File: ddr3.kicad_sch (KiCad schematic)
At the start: 22 parts, among them U101 xc7z010clg400, U201 MT41K256M16TW-107_P

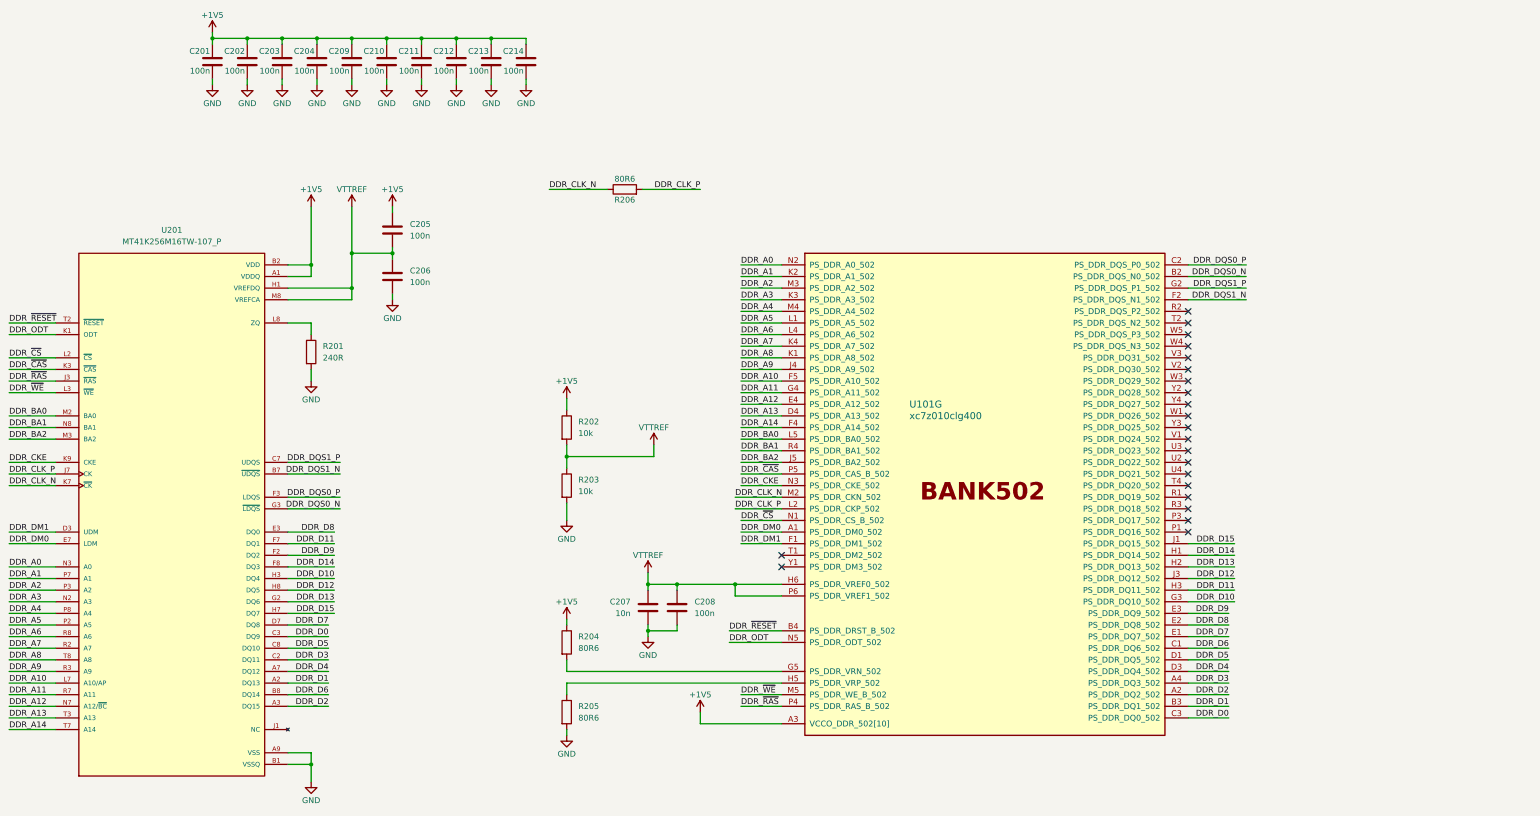
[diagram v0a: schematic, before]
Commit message: feat: add serial res
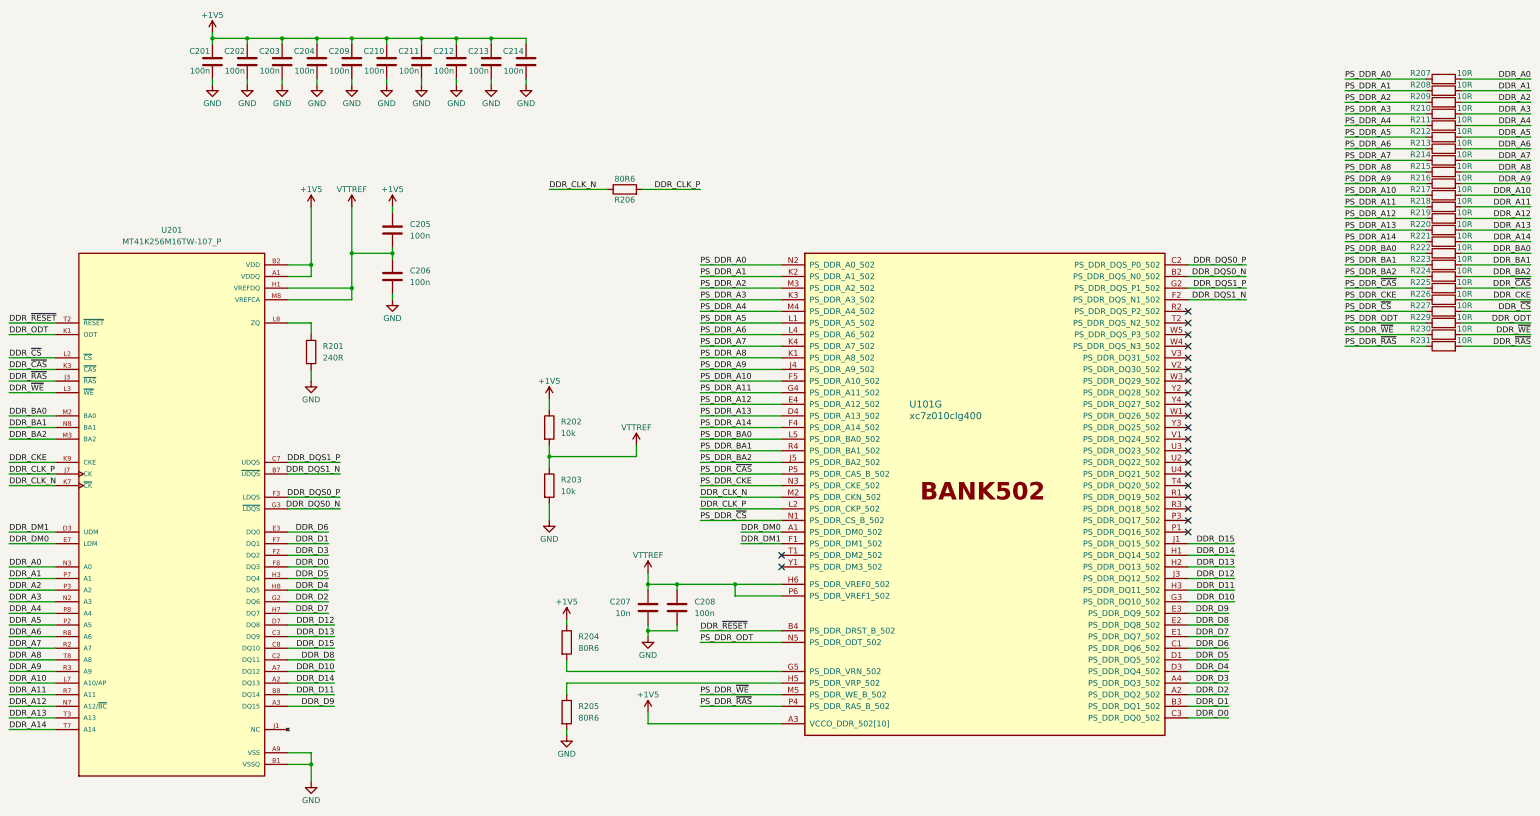
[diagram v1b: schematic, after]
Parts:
- added R207, R208, R209, R210, R211, R212, R213, R214, R215, R216, R217, R218, R219, R220, R221, R222, R223, R224, R225, R226, R227, R229, R230, R231: 10R, Resistor_SMD:R_0402_1005Metric, symbol Device:R
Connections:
- net DDR_A0: now also R207.2; no longer U101.N2 (PS_DDR_A0_502)
- net DDR_A1: now also R208.2; no longer U101.K2 (PS_DDR_A1_502)
- net DDR_A10: now also R217.2; no longer U101.F5 (PS_DDR_A10_502)
- net DDR_A11: now also R218.2; no longer U101.G4 (PS_DDR_A11_502)
- net DDR_A12: now also R219.2; no longer U101.E4 (PS_DDR_A12_502)
- net DDR_A13: now also R220.2; no longer U101.D4 (PS_DDR_A13_502)
- net DDR_A14: now also R221.2; no longer U101.F4 (PS_DDR_A14_502)
- net DDR_A2: now also R209.2; no longer U101.M3 (PS_DDR_A2_502)
- net DDR_A3: now also R210.2; no longer U101.K3 (PS_DDR_A3_502)
- net DDR_A4: now also R211.2; no longer U101.M4 (PS_DDR_A4_502)
- net DDR_A5: now also R212.2; no longer U101.L1 (PS_DDR_A5_502)
- net DDR_A6: now also R213.2; no longer U101.L4 (PS_DDR_A6_502)
- net DDR_A7: now also R214.2; no longer U101.K4 (PS_DDR_A7_502)
- net DDR_A8: now also R215.2; no longer U101.K1 (PS_DDR_A8_502)
- net DDR_A9: now also R216.2; no longer U101.J4 (PS_DDR_A9_502)
- net DDR_BA0: now also R222.2; no longer U101.L5 (PS_DDR_BA0_502)
- net DDR_BA1: now also R223.2; no longer U101.R4 (PS_DDR_BA1_502)
- net DDR_BA2: now also R224.2; no longer U101.J5 (PS_DDR_BA2_502)
- net DDR_CKE: now also R226.2; no longer U101.N3 (PS_DDR_CKE_502)
- net DDR_D0: now also U201.F8 (DQ3); no longer U201.C3 (DQ9)
- net DDR_D1: now also U201.F7 (DQ1); no longer U201.A2 (DQ13)
- net DDR_D10: now also U201.A7 (DQ12); no longer U201.H3 (DQ4)
- net DDR_D11: now also U201.B8 (DQ14); no longer U201.F7 (DQ1)
- net DDR_D12: now also U201.D7 (DQ8); no longer U201.H8 (DQ5)
- net DDR_D13: now also U201.C3 (DQ9); no longer U201.G2 (DQ6)
- net DDR_D14: now also U201.A2 (DQ13); no longer U201.F8 (DQ3)
- net DDR_D15: now also U201.C8 (DQ10); no longer U201.H7 (DQ7)
- net DDR_D2: now also U201.G2 (DQ6); no longer U201.A3 (DQ15)
- net DDR_D3: now also U201.F2 (DQ2); no longer U201.C2 (DQ11)
- net DDR_D4: now also U201.H8 (DQ5); no longer U201.A7 (DQ12)
- net DDR_D5: now also U201.H3 (DQ4); no longer U201.C8 (DQ10)
- net DDR_D6: now also U201.E3 (DQ0); no longer U201.B8 (DQ14)
- net DDR_D7: now also U201.H7 (DQ7); no longer U201.D7 (DQ8)
- net DDR_D8: now also U201.C2 (DQ11); no longer U201.E3 (DQ0)
- net DDR_D9: now also U201.A3 (DQ15); no longer U201.F2 (DQ2)
- net DDR_ODT: now also R229.2; no longer U101.N5 (PS_DDR_ODT_502)
- net DDR_~{CAS}: now also R225.2; no longer U101.P5 (PS_DDR_CAS_B_502)
- net DDR_~{CS}: now also R227.2; no longer U101.N1 (PS_DDR_CS_B_502)
- net DDR_~{RAS}: now also R231.2; no longer U101.P4 (PS_DDR_RAS_B_502)
- net DDR_~{WE}: now also R230.2; no longer U101.M5 (PS_DDR_WE_B_502)
- new net PS_DDR_A0: R207.1, U101.N2 (PS_DDR_A0_502)
- new net PS_DDR_A1: R208.1, U101.K2 (PS_DDR_A1_502)
- new net PS_DDR_A10: R217.1, U101.F5 (PS_DDR_A10_502)
- new net PS_DDR_A11: R218.1, U101.G4 (PS_DDR_A11_502)
- new net PS_DDR_A12: R219.1, U101.E4 (PS_DDR_A12_502)
- new net PS_DDR_A13: R220.1, U101.D4 (PS_DDR_A13_502)
- new net PS_DDR_A14: R221.1, U101.F4 (PS_DDR_A14_502)
- new net PS_DDR_A2: R209.1, U101.M3 (PS_DDR_A2_502)
- new net PS_DDR_A3: R210.1, U101.K3 (PS_DDR_A3_502)
- new net PS_DDR_A4: R211.1, U101.M4 (PS_DDR_A4_502)
- new net PS_DDR_A5: R212.1, U101.L1 (PS_DDR_A5_502)
- new net PS_DDR_A6: R213.1, U101.L4 (PS_DDR_A6_502)
- new net PS_DDR_A7: R214.1, U101.K4 (PS_DDR_A7_502)
- new net PS_DDR_A8: R215.1, U101.K1 (PS_DDR_A8_502)
- new net PS_DDR_A9: R216.1, U101.J4 (PS_DDR_A9_502)
- new net PS_DDR_BA0: R222.1, U101.L5 (PS_DDR_BA0_502)
- new net PS_DDR_BA1: R223.1, U101.R4 (PS_DDR_BA1_502)
- new net PS_DDR_BA2: R224.1, U101.J5 (PS_DDR_BA2_502)
- new net PS_DDR_CKE: R226.1, U101.N3 (PS_DDR_CKE_502)
- new net PS_DDR_ODT: R229.1, U101.N5 (PS_DDR_ODT_502)
- new net PS_DDR_~{CAS}: R225.1, U101.P5 (PS_DDR_CAS_B_502)
- new net PS_DDR_~{CS}: R227.1, U101.N1 (PS_DDR_CS_B_502)
- new net PS_DDR_~{RAS}: R231.1, U101.P4 (PS_DDR_RAS_B_502)
- new net PS_DDR_~{WE}: R230.1, U101.M5 (PS_DDR_WE_B_502)
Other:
- moved on the sheet: R202, R203

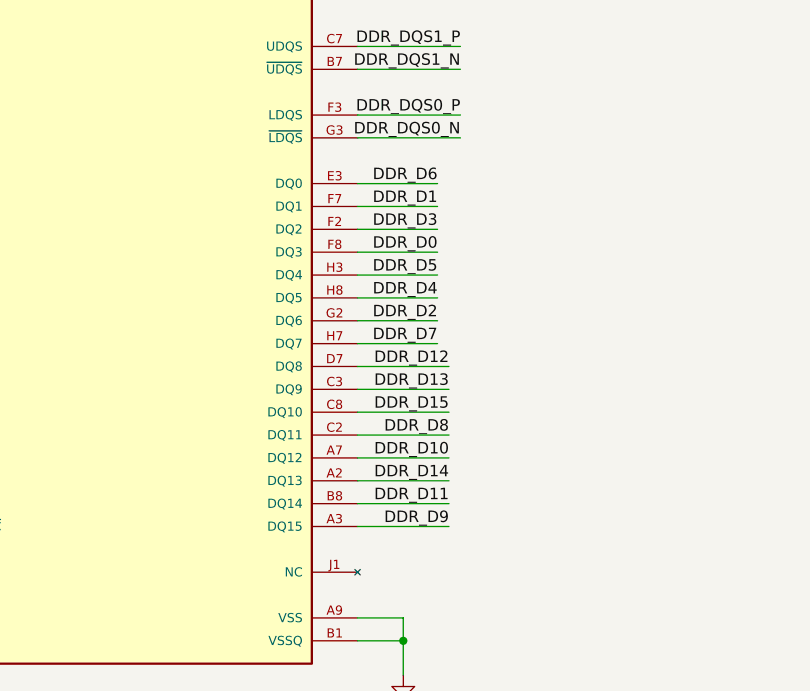
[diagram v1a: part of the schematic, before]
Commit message: feat: finish basic ddr3 routing
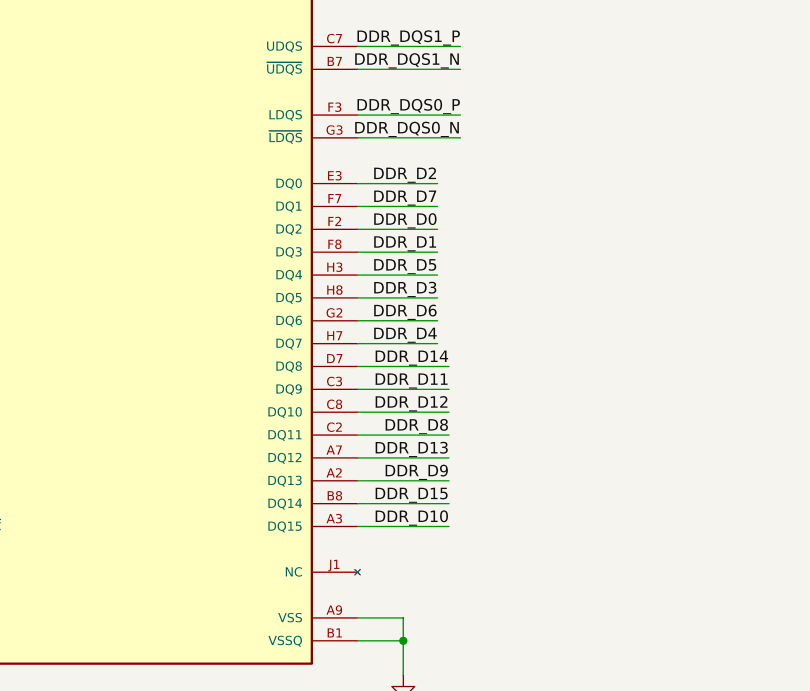
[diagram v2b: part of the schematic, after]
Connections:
- net DDR_D0: now also U201.F2 (DQ2); no longer U201.F8 (DQ3)
- net DDR_D1: now also U201.F8 (DQ3); no longer U201.F7 (DQ1)
- net DDR_D10: now also U201.A3 (DQ15); no longer U201.A7 (DQ12)
- net DDR_D11: now also U201.C3 (DQ9); no longer U201.B8 (DQ14)
- net DDR_D12: now also U201.C8 (DQ10); no longer U201.D7 (DQ8)
- net DDR_D13: now also U201.A7 (DQ12); no longer U201.C3 (DQ9)
- net DDR_D14: now also U201.D7 (DQ8); no longer U201.A2 (DQ13)
- net DDR_D15: now also U201.B8 (DQ14); no longer U201.C8 (DQ10)
- net DDR_D2: now also U201.E3 (DQ0); no longer U201.G2 (DQ6)
- net DDR_D3: now also U201.H8 (DQ5); no longer U201.F2 (DQ2)
- net DDR_D4: now also U201.H7 (DQ7); no longer U201.H8 (DQ5)
- net DDR_D6: now also U201.G2 (DQ6); no longer U201.E3 (DQ0)
- net DDR_D7: now also U201.F7 (DQ1); no longer U201.H7 (DQ7)
- net DDR_D9: now also U201.A2 (DQ13); no longer U201.A3 (DQ15)
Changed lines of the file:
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@@
 	)
 	(label "DDR_D1"
-		(at 121.92 143.51 180)
+		(at 121.92 148.59 180)
 		(effects
 			(font
@@
 	)
 	(label "DDR_D10"
-		(at 123.19 171.45 180)
+		(at 123.19 179.07 180)
 		(effects
 			(font
@@
 	)
 	(label "DDR_D6"
-		(at 121.92 140.97 180)
+		(at 121.92 156.21 180)
 		(effects
 			(font
@@
 	)
 	(label "DDR_D2"
-		(at 121.92 156.21 180)
+		(at 121.92 140.97 180)
 		(effects
 			(font
@@
 	)
 	(label "DDR_D4"
-		(at 121.92 153.67 180)
+		(at 121.92 158.75 180)
 		(effects
 			(font
@@
 	)
 	(label "DDR_D11"
-		(at 123.19 176.53 180)
+		(at 123.19 163.83 180)
 		(effects
 			(font
@@
 	)
 	(label "DDR_D15"
-		(at 123.19 166.37 180)
+		(at 123.19 176.53 180)
 		(effects
 			(font
@@
 	)
 	(label "DDR_D0"
-		(at 121.92 148.59 180)
+		(at 121.92 146.05 180)
 		(effects
 			(font
@@
 	)
 	(label "DDR_D12"
-		(at 123.19 161.29 180)
+		(at 123.19 166.37 180)
 		(effects
 			(font
@@
 	)
 	(label "DDR_D7"
-		(at 121.92 158.75 180)
+		(at 121.92 143.51 180)
 		(effects
 			(font
@@
 	)
 	(label "DDR_D3"
-		(at 121.92 146.05 180)
+		(at 121.92 153.67 180)
 		(effects
 			(font
@@
 	)
 	(label "DDR_D9"
-		(at 123.19 179.07 180)
+		(at 123.19 173.99 180)
 		(effects
 			(font
@@
 	)
 	(label "DDR_D14"
-		(at 123.19 173.99 180)
+		(at 123.19 161.29 180)
 		(effects
 			(font
@@
 	)
 	(label "DDR_D13"
-		(at 123.19 163.83 180)
-		(effects
-			(font
+		(at 123.19 171.45 180)
+		(effects
+			(font

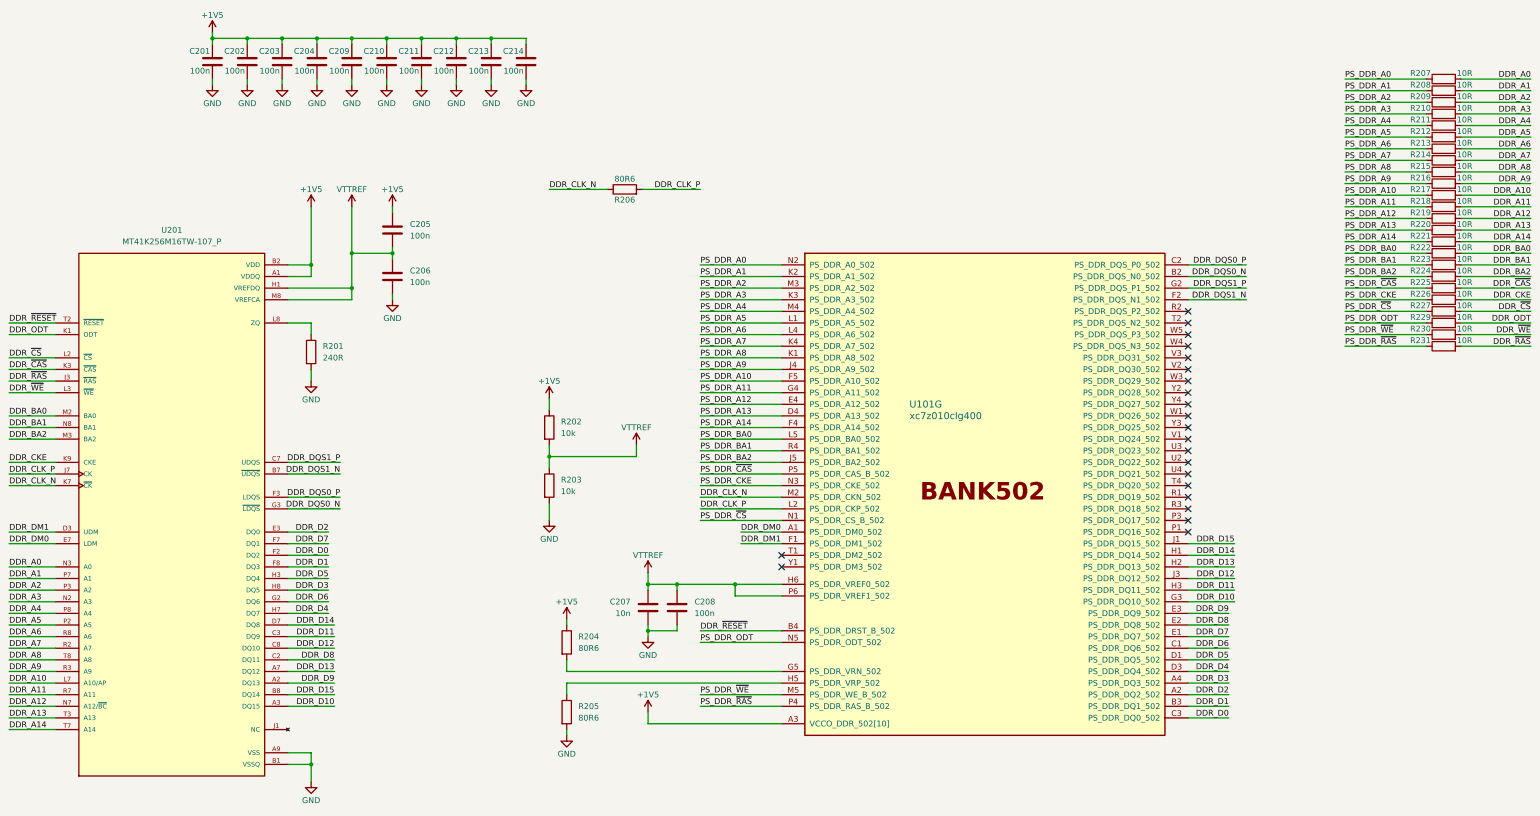
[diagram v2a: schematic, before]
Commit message: feat: continue routing ddr3
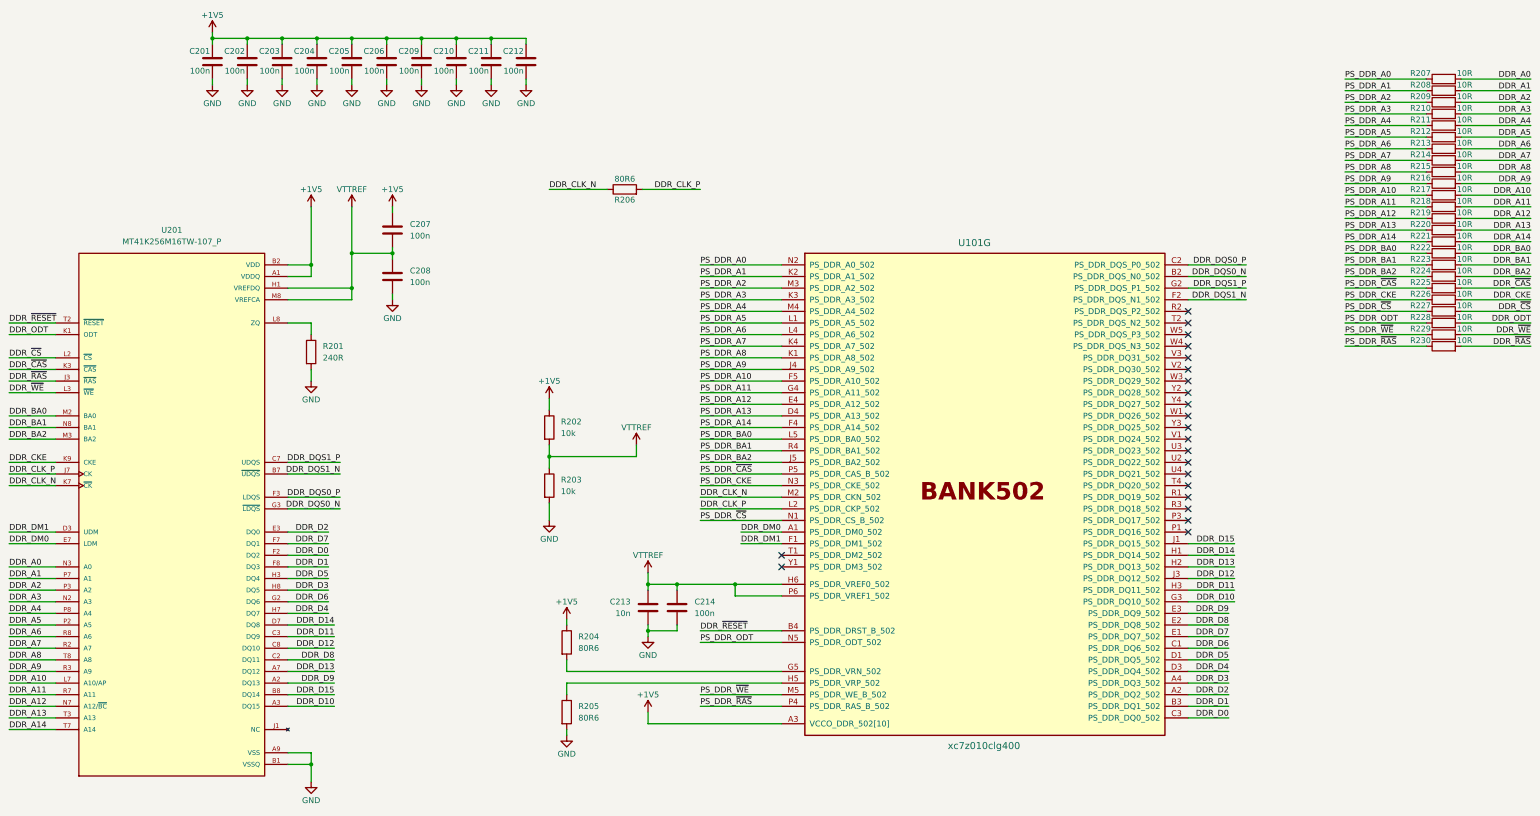
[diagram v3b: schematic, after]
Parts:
- C213: renamed from C207; footprint (none) -> Capacitor_SMD:C_0402_1005Metric
- renumbered C209 to C205, C210 to C206, C205 to C207, C206 to C208, C211 to C209, C212 to C210, C213 to C211, C214 to C212, C208 to C214, R229 to R228, R230 to R229, R231 to R230
